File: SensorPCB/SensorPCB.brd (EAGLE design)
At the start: 36 x 66 mm, 31 parts, among them T1 33u

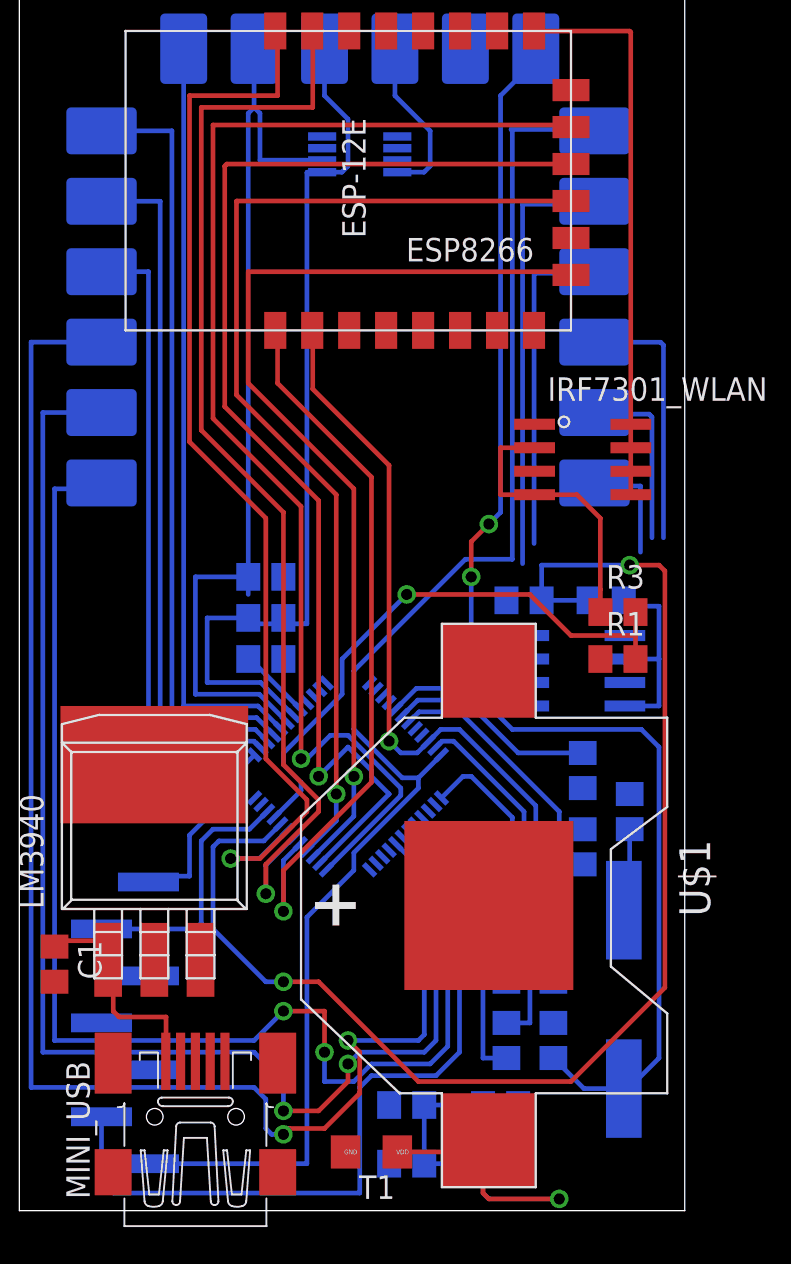
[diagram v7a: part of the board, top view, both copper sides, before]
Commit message: routed all signal wires, 3v and GND are absent
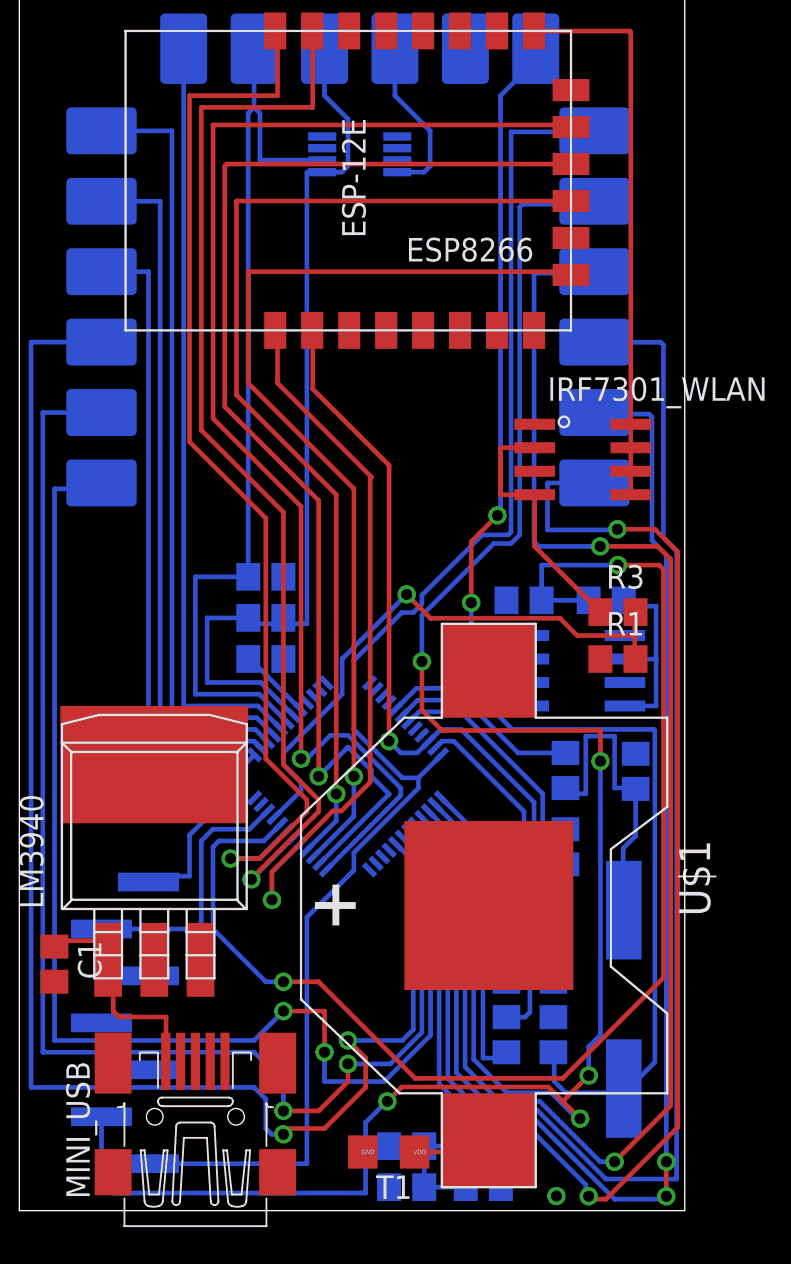
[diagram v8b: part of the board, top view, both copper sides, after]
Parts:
- moved C7 2.41 mm to (25.1, 3.49)
- moved C5 2.22 mm to (21.0, 3.49)
- moved C6 2.20 mm to (33.3, 23.8)
- moved C8 1.58 mm to (25.1, 1.27)
- moved C3 1.27 mm to (21.0, 1.27)
- moved C10 0.93 mm to (29.5, 19.7)
- moved R11 0.93 mm to (29.5, 23.8)
- moved T1 0.93 mm to (20.0, 3.17)
- moved C4 0.31 mm to (28.9, 9.52)
- moved R7 0.31 mm to (26.4, 9.52)
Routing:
- net PA7: track 6.45 -> 75.8 mm, vias 0 -> 2
- net PA4: track 18.0 -> 84.7 mm, vias 0 -> 2
- net PA6: track 9.75 -> 75.1 mm, vias 0 -> 2
- net PA5: track 14.2 -> 78.3 mm
- net USART2_RX_SENSOR: track 73.6 -> 122.6 mm, vias 0 -> 5
- net +3V3: track 37.2 -> 22.2 mm
- net N$4: track 4.96 -> 17.2 mm
- net OSC_IN: track 39.9 -> 41.6 mm
- net PB0: track 71.6 -> 69.9 mm
- net GATE_WLAN: track 15.8 -> 14.5 mm
- net PB1: track 75.2 -> 73.9 mm
- net I2C1_SCL_SENSOR: track 50.8 -> 49.9 mm
- net OSC_OUT: track 11.3 -> 10.4 mm
- net USART1_TX_WLAN: track 60.2 -> 59.3 mm
- net PB2: track 83.2 -> 82.4 mm
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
